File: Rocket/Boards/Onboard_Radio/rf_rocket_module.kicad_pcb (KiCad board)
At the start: 4 copper layers, 65 x 50 mm, 91 parts, among them J10 M80, J11 MICROFIT, J3 USB_B_Micro, J4 SWD JST PH, J5 MICROFIT, J6 RFIO SMA, J9 M80, U1 TCAN1046, U2 SX1262, U3 PE4259 RF Switch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

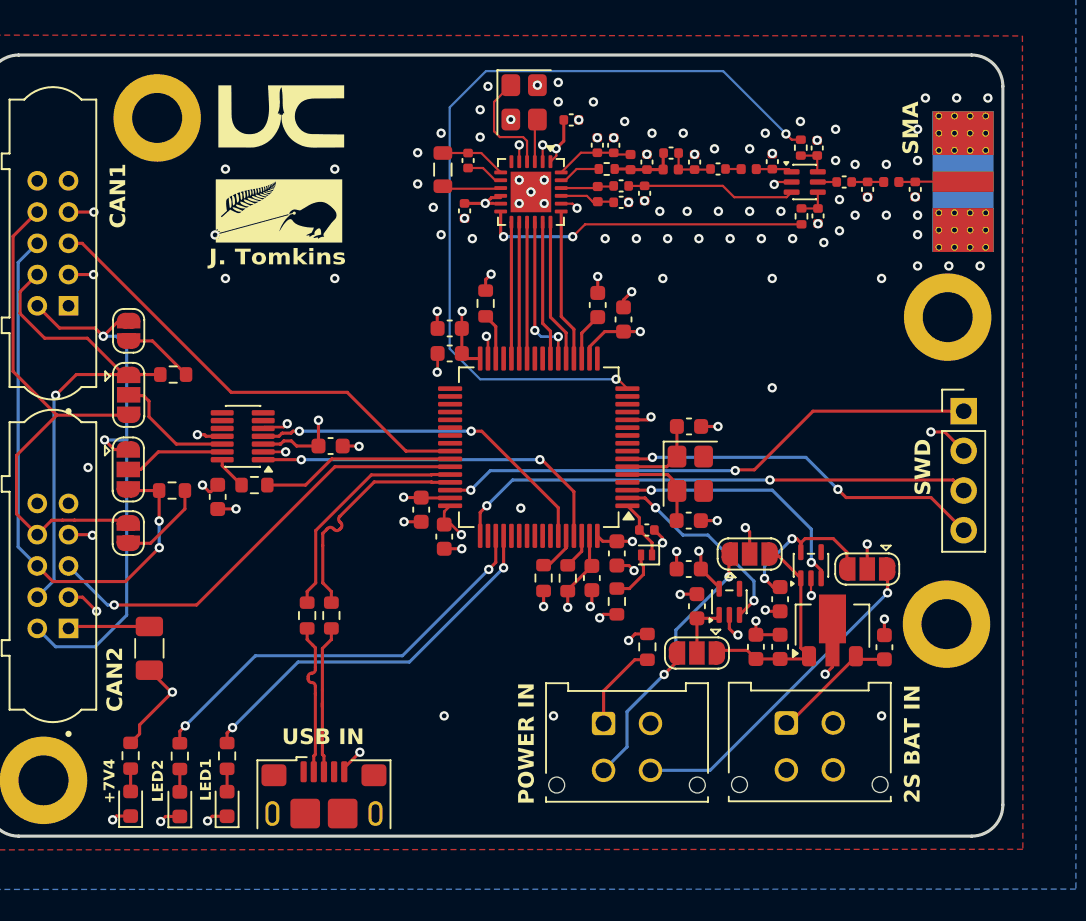
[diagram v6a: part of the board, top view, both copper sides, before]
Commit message: updated swd and crystal
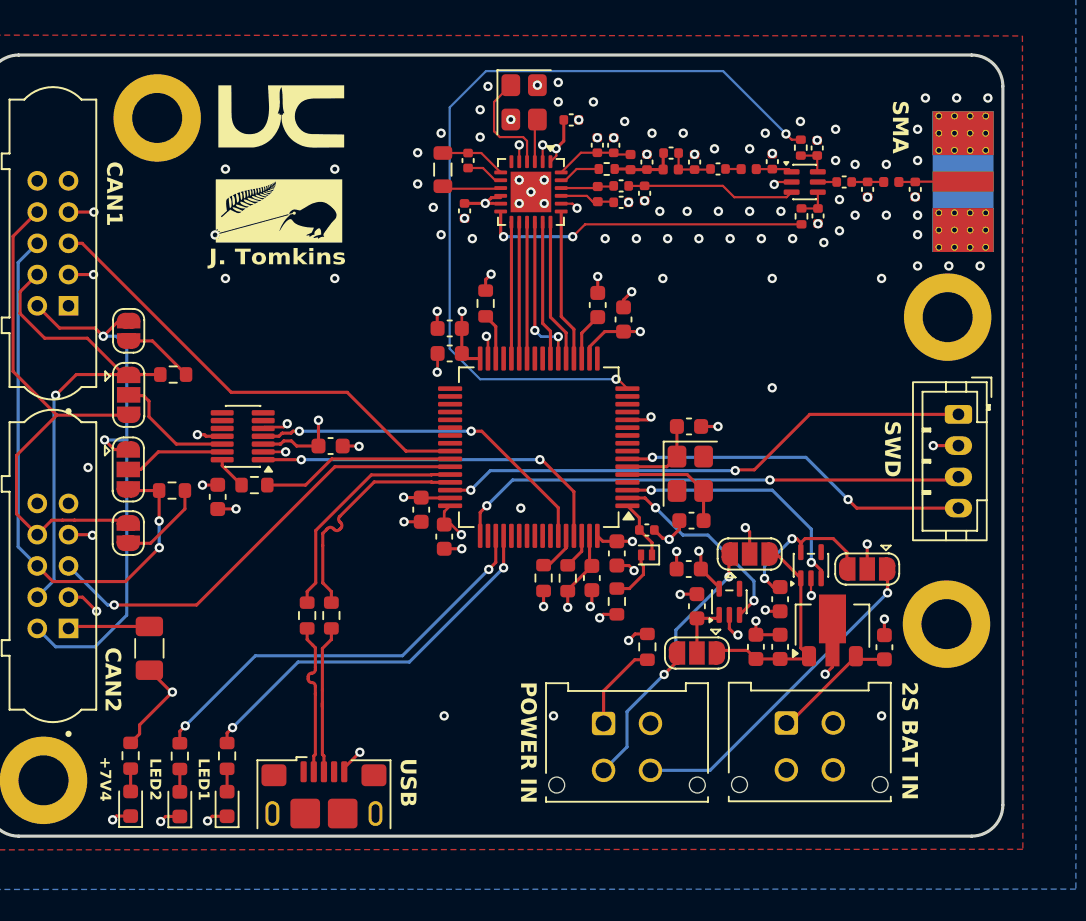
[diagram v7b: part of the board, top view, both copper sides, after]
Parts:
- J4: footprint Connector_PinHeader_2.54mm:PinHeader_1x04_P2.54mm_Vertical -> Connector_JST:JST_PH_B4B-PH-K_1x04_P2.00mm_Vertical
- moved J4 0.39 mm to (187.1, 110.0), turned to -90 degrees
- moved C31 0.18 mm to (170.0, 116.8), turned to 0 degrees
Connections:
- Y2 pad 2: Net-(U4-PH0) -> (no net)
- Y2 pad 3: (no net) -> Net-(U4-PH0)
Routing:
- net /+3V3A: track 47.5 -> 43.8 mm
- net Net-(U4-PH0): track 5.78 -> 7.21 mm
- net /MCU/NRST: track 23.5 -> 22.6 mm
- net +5V: track 52.3 -> 51.7 mm
- net /MCU/SWDIO: track 33.6 -> 33.1 mm
- net GND: track 71.5 -> 71.8 mm, vias 122 -> 121
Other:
- board text added: "USB"
- board text removed: "USB IN"
